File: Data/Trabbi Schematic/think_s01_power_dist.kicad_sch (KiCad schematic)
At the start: 3 parts, among them SW1 Ignition Switch

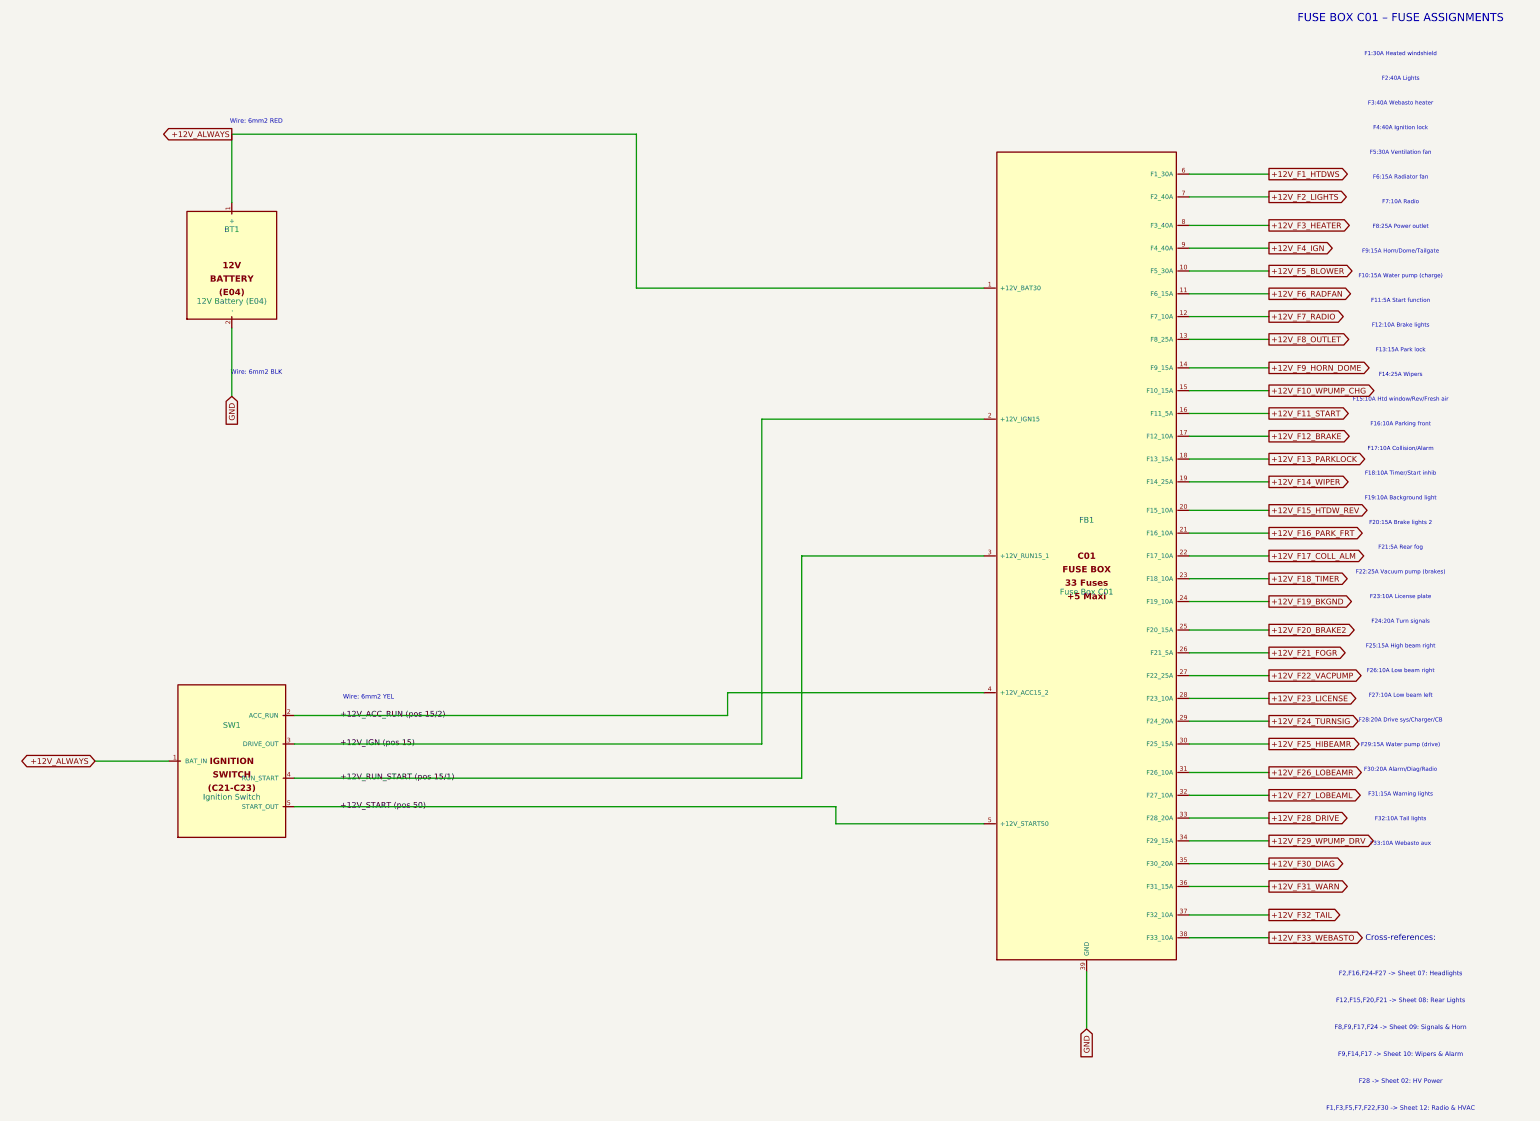
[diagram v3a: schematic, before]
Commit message: Fix label/text positioning: Ref/Value outside body, hide pin numbers
- Reference placed above body edge, Value below (dynamic based on
  symbol height) — no longer overlapping body text
- Pin numbers hidden (clutter, not useful in schematic view)
- Pin name font reduced from 1.016mm to 0.762mm (less overlap)
- Pin length increased from 2.54mm to 3.81mm (more room for pin names
  between body edge and endpoint)
- Store symbol dimensions in _sym_dims for dynamic property placement

Co-Authored-By: Claude Opus 4.6 <noreply@anthropic.com>
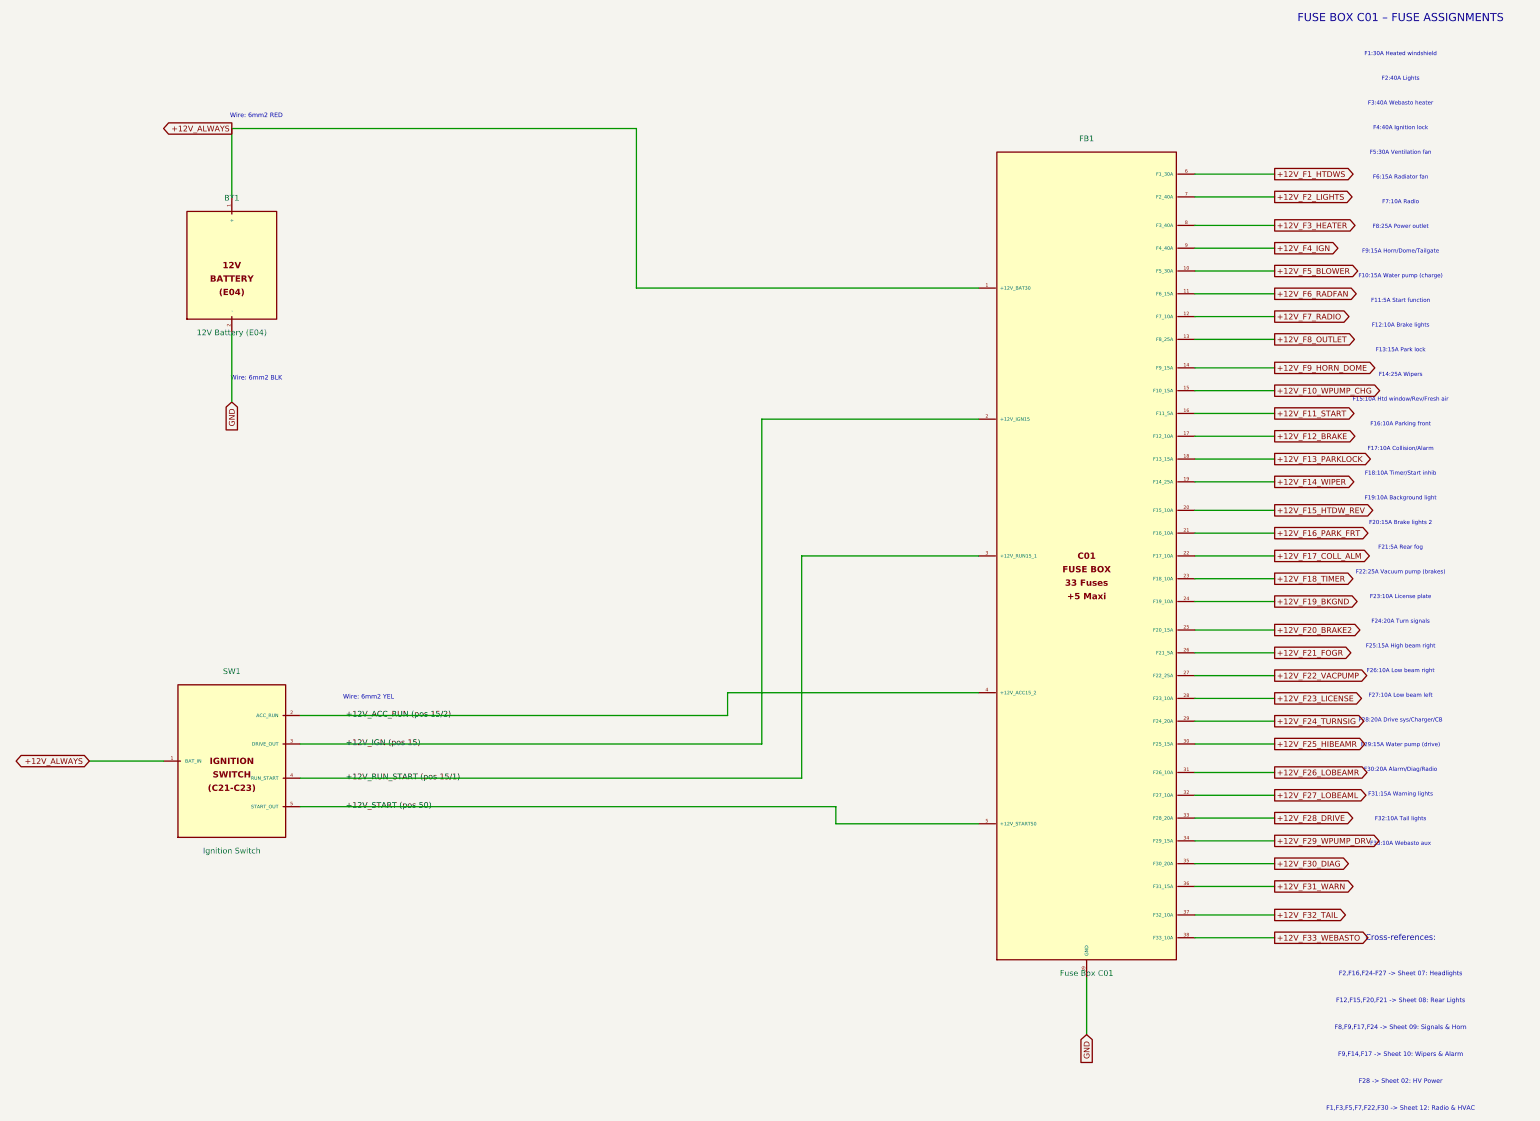
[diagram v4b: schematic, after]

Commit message: Add cross-sheet reference annotations to global labels
- Track all global label positions per sheet during build
- After building all sheets, annotate each global label with
  "→S01,S03,..." text showing which other sheets share the net
- 60 cross-sheet nets identified and annotated
- Two-pass build: 1) build all sheets 2) add cross-refs + save
- Text placed near label in 0.8mm font, offset to avoid overlap

Co-Authored-By: Claude Opus 4.6 <noreply@anthropic.com>
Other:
- note added: "→S02,S03,S04,S05,S06,S07,S08,S09,S10,S11,S12,S13"
- note added: "→S02,S06,S13"
- note added: "→S05,S11"
- note added: "→S06"
- note added: "→S06,S11"
- note added: "→S07"
- note added: "→S07,S10,S11,S13"
- note added: "→S08"
- note added: "→S09"
- note added: "→S09,S10,S12"
- note added: "→S10"
- note added: "→S11"
- note added: "→S12"
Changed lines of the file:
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@@
     (effects (font (size 1.000 1.000)))
+  )
+  (text "→S05,S11" (at 46.530 52.030 0)
+    (effects (font (size 0.800 0.800)))
+  )
+  (text "→S05,S11" (at 14.780 193.000 0)
+    (effects (font (size 0.800 0.800)))
+  )
+  (text "→S02,S03,S04,S05,S06,S07,S08,S09,S10,S11,S12,S13" (at 52.530 112.490 0)
+    (effects (font (size 0.800 0.800)))
+  )
+  (text "→S02,S03,S04,S05,S06,S07,S08,S09,S10,S11,S12,S13" (at 243.030 253.460 0)
+    (effects (font (size 0.800 0.800)))
+  )
+  (text "→S12" (at 284.940 62.190 0)
+    (effects (font (size 0.800 0.800)))
+  )
+  (text "→S07" (at 284.940 67.270 0)
+    (effects (font (size 0.800 0.800)))
+  )
+  (text "→S12" (at 284.940 73.620 0)
+    (effects (font (size 0.800 0.800)))
+  )
+  (text "→S12" (at 284.940 83.780 0)
+    (effects (font (size 0.800 0.800)))
+  )
+  (text "→S06" (at 284.940 88.860 0)
+    (effects (font (size 0.800 0.800)))
+  )
+  (text "→S12" (at 284.940 93.940 0)
+    (effects (font (size 0.800 0.800)))
+  )
+  (text "→S09" (at 284.940 99.020 0)
+    (effects (font (size 0.800 0.800)))
+  )
+  (text "→S09,S10,S12" (at 284.940 105.370 0)
+    (effects (font (size 0.800 0.800)))
+  )
+  (text "→S06,S11" (at 284.940 110.450 0)
+    (effects (font (size 0.800 0.800)))
+  )
+  (text "→S08" (at 284.940 120.610 0)
+    (effects (font (size 0.800 0.800)))
+  )
+  (text "→S10" (at 284.940 130.770 0)
+    (effects (font (size 0.800 0.800)))
+  )
+  (text "→S08" (at 284.940 137.120 0)
+    (effects (font (size 0.800 0.800)))
+  )
+  (text "→S07" (at 284.940 142.200 0)
+    (effects (font (size 0.800 0.800)))
+  )
+  (text "→S07,S10,S11,S13" (at 284.940 147.280 0)
+    (effects (font (size 0.800 0.800)))
+  )
+  (text "→S08" (at 284.940 163.790 0)
+    (effects (font (size 0.800 0.800)))
+  )
+  (text "→S08" (at 284.940 168.870 0)
+    (effects (font (size 0.800 0.800)))
+  )
+  (text "→S12" (at 284.940 173.950 0)
+    (effects (font (size 0.800 0.800)))
+  )
+  (text "→S07" (at 284.940 179.030 0)
+    (effects (font (size 0.800 0.800)))
+  )
+  (text "→S09" (at 284.940 184.110 0)
+    (effects (font (size 0.800 0.800)))
+  )
+  (text "→S07" (at 284.940 189.190 0)
+    (effects (font (size 0.800 0.800)))
+  )
+  (text "→S07" (at 284.940 195.540 0)
+    (effects (font (size 0.800 0.800)))
+  )
+  (text "→S07" (at 284.940 200.620 0)
+    (effects (font (size 0.800 0.800)))
+  )
+  (text "→S02,S06,S13" (at 284.940 205.700 0)
+    (effects (font (size 0.800 0.800)))
+  )
+  (text "→S11" (at 284.940 215.860 0)
+    (effects (font (size 0.800 0.800)))
+  )
+  (text "→S12" (at 284.940 232.370 0)
+    (effects (font (size 0.800 0.800)))
   )
   (symbol_instances)

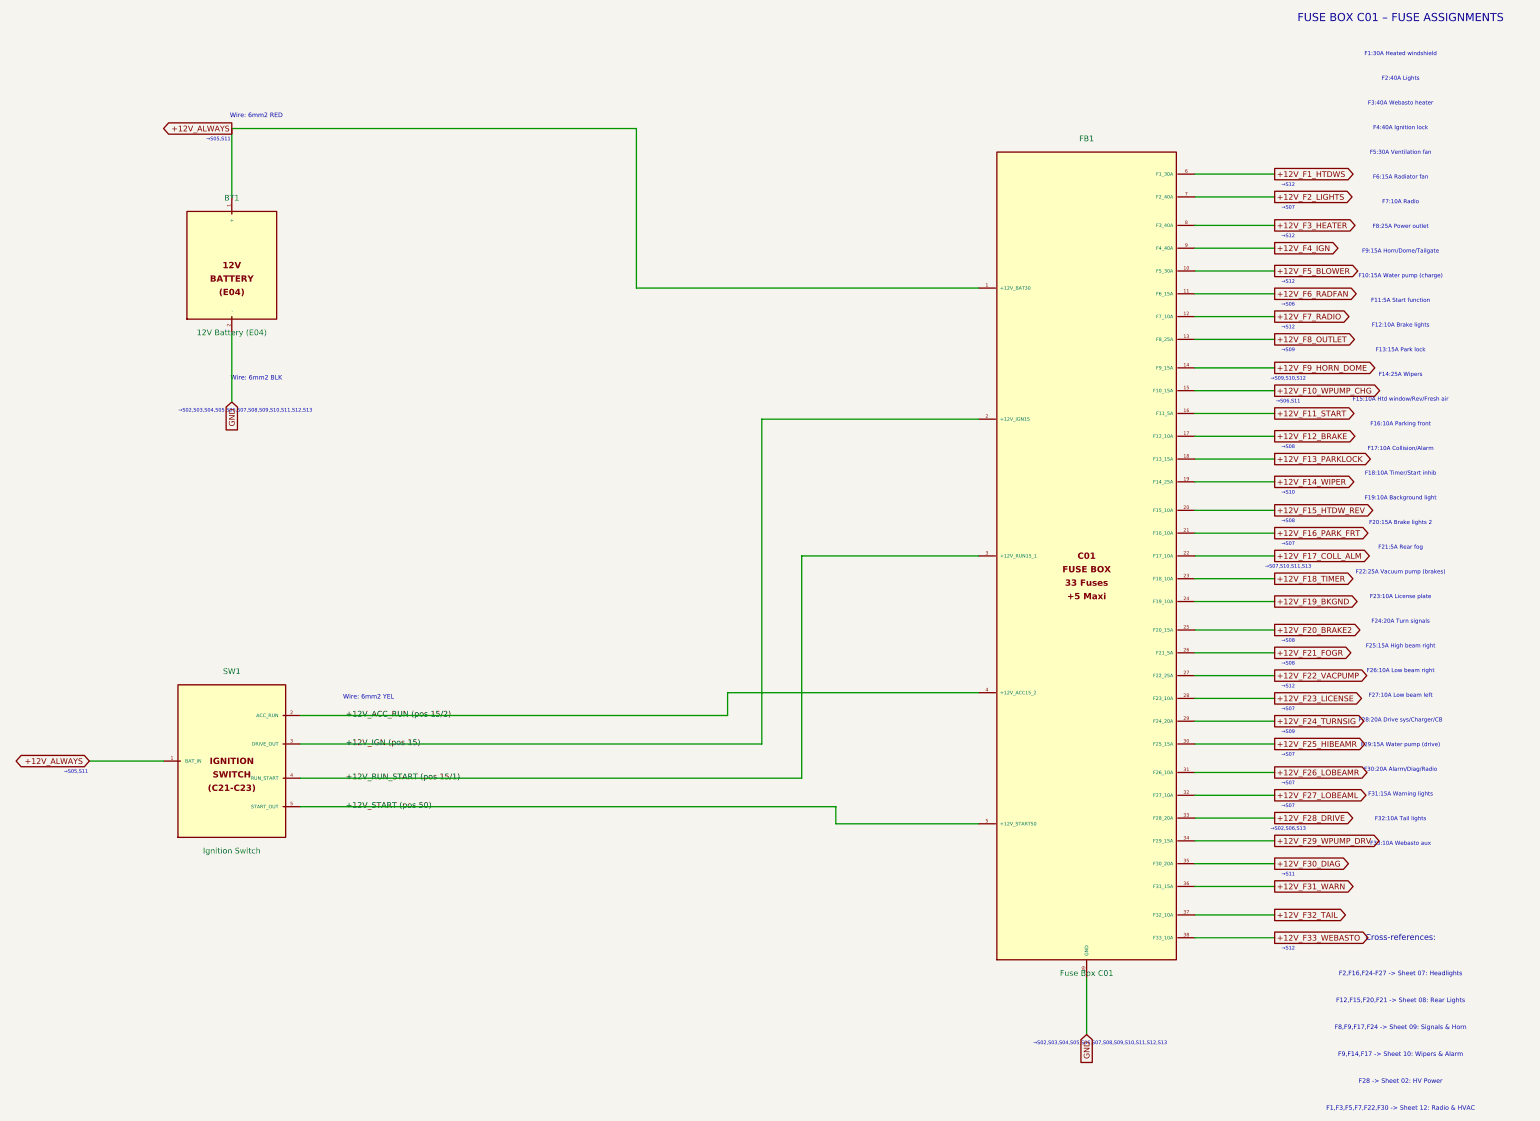
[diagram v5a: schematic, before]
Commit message: Fix label text justification for KiCad 9
Add (justify left) to all label and global_label effects.
KiCad 9 requires explicit text justification — without it,
label text is mispositioned relative to the label shape.

Co-Authored-By: Claude Opus 4.6 <noreply@anthropic.com>
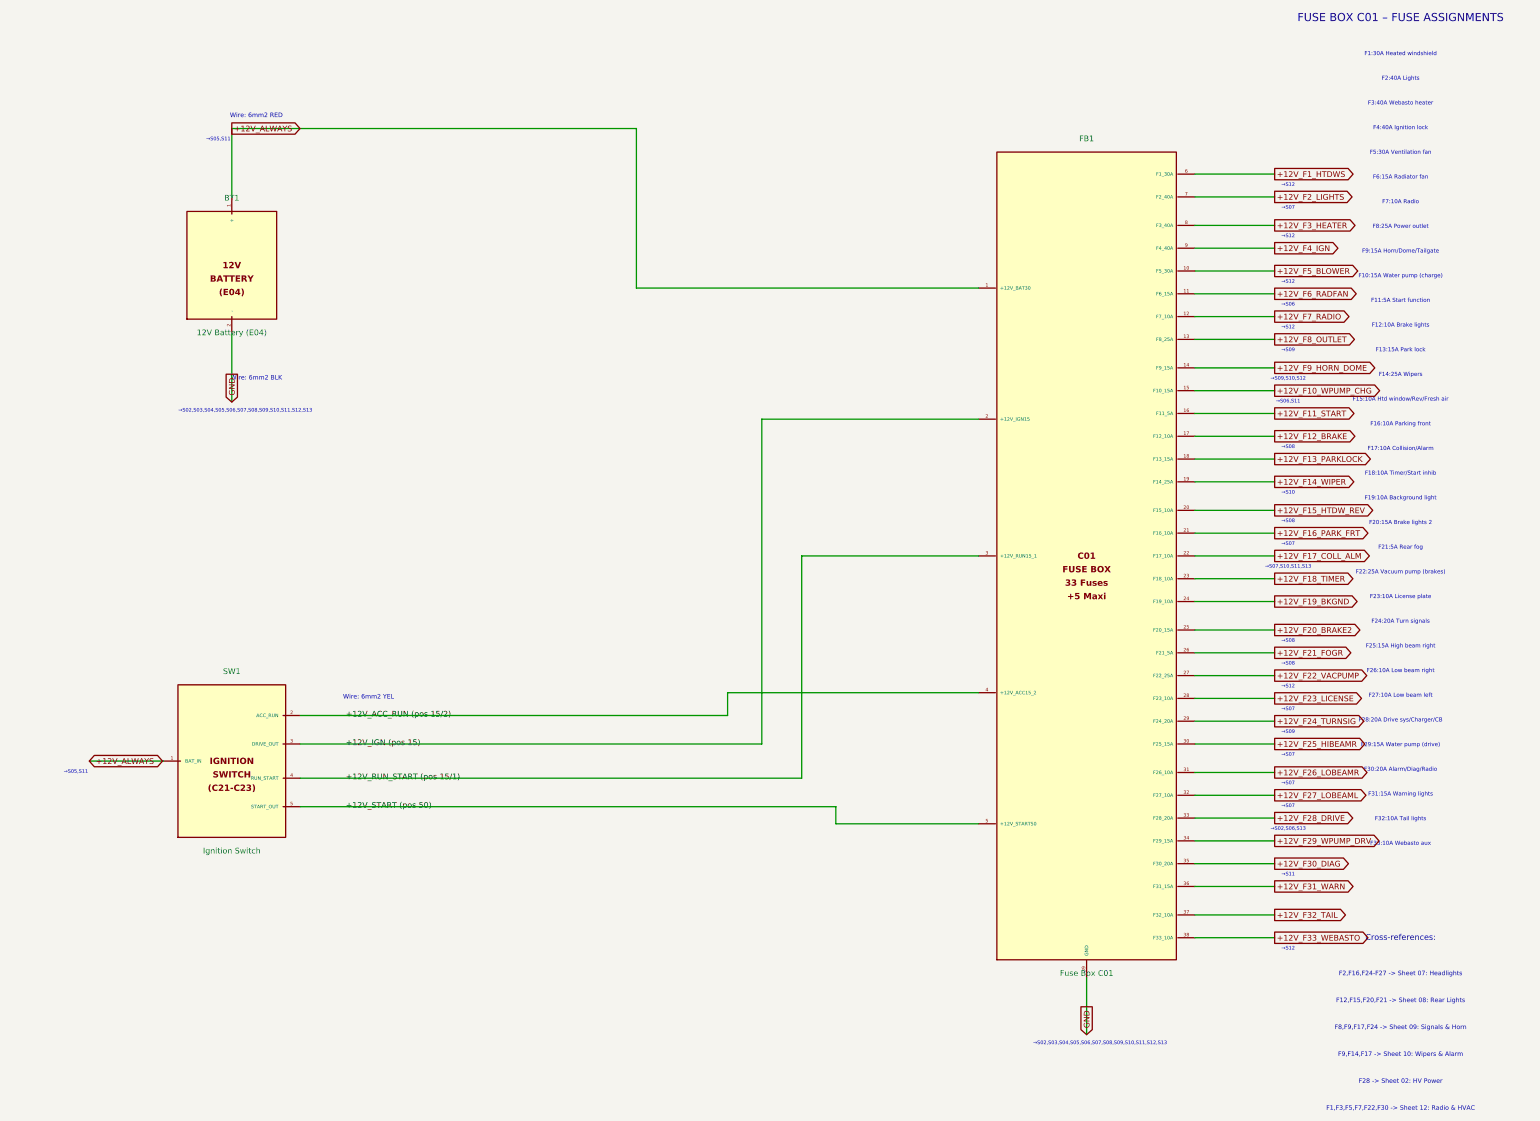
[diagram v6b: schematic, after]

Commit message: Relay symbol for flasher, label justify set to auto
- Flasher Relay (Think:FLASHER_RELAY) now has coil+switch graphics
  matching the standard relay symbol style
- All relays (SPST, SPDT, Flasher) use consistent coil+switch body
- Remove (justify left) from all label and global_label effects —
  KiCad 9 auto-determines text alignment based on label orientation

Co-Authored-By: Claude Opus 4.6 <noreply@anthropic.com>
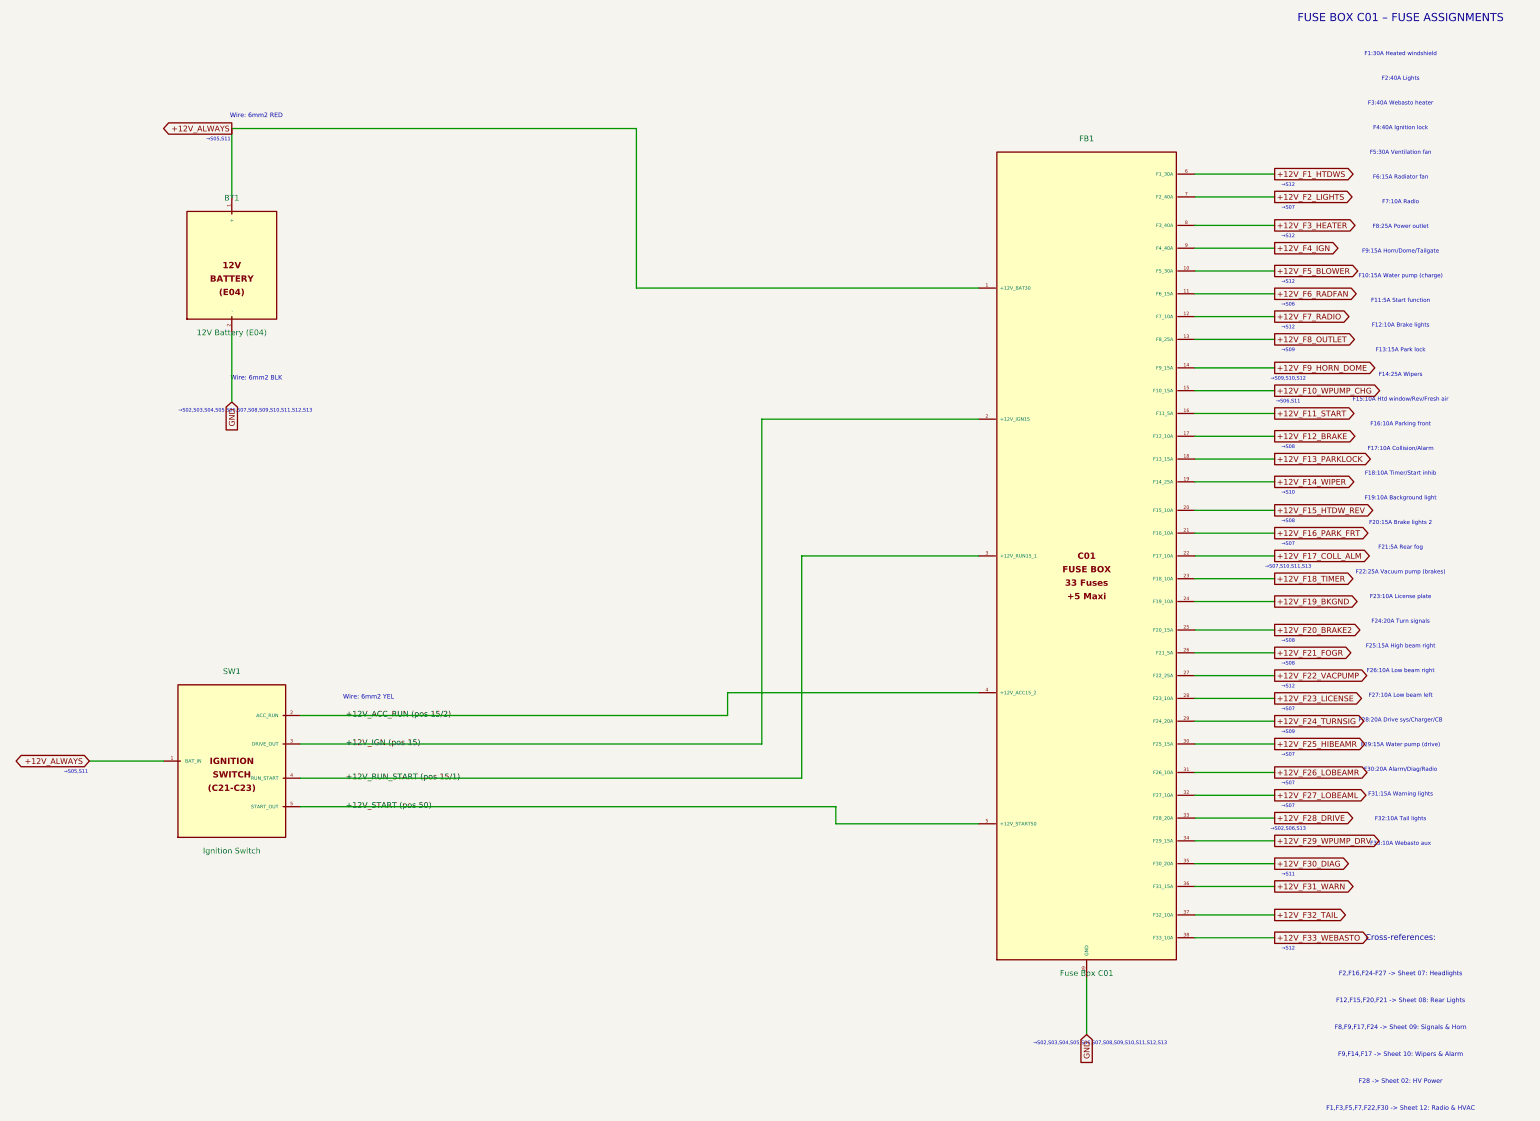
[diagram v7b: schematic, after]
